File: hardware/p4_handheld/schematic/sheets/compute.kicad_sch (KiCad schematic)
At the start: 0 parts

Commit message: hw(p4_handheld): compute cluster ported, diffs clean vs card
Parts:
- added L1: 2.2uH, IND-SMD_L4.0-W4.0_HPC4018BM, symbol PSP4H:Block2
- added R3, R4: 4.7k, R0402, symbol Device:R
- added R5, R6: 10k, R0402, symbol Device:R
- added U1: ESP32-P4NRW32X, QFN-104_L10.0-W10.0-P0.35-TL-EP7.5, symbol PSP4H:Block2
- added U9: QSPI-NOR-32MB, WSON-8_L8.0-W6.10-P1.27-BL-EP, symbol PSP4H:Block2
- added X1: 40MHz-crystal, SMD3225-4P, symbol PSP4H:Block2

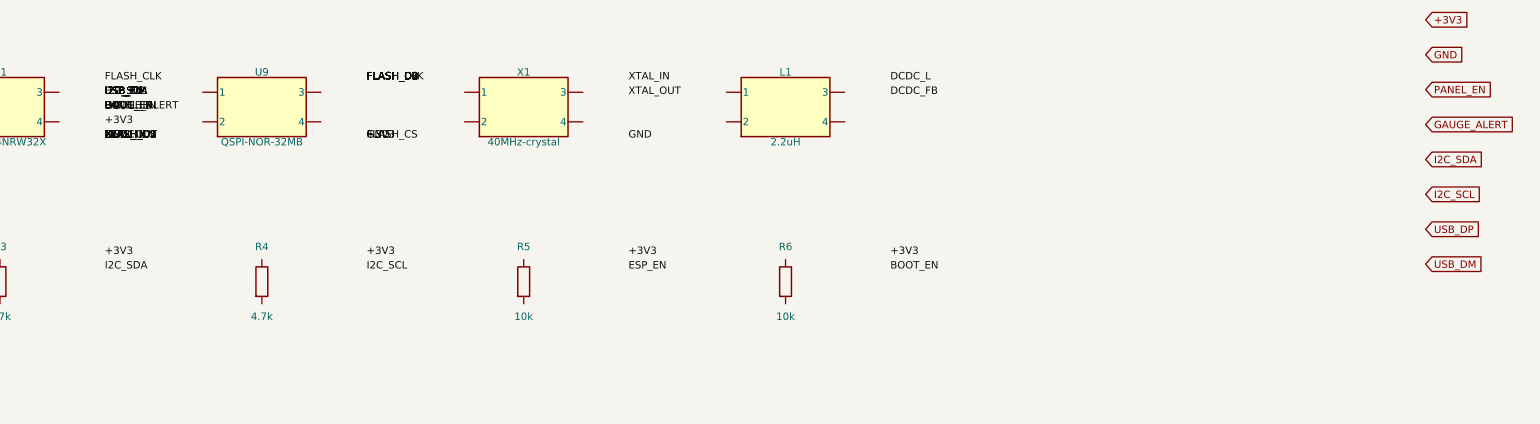
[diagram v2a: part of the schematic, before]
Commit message: hw(p4_handheld): display sheet wired to Waveshare 2.8in DSI panel
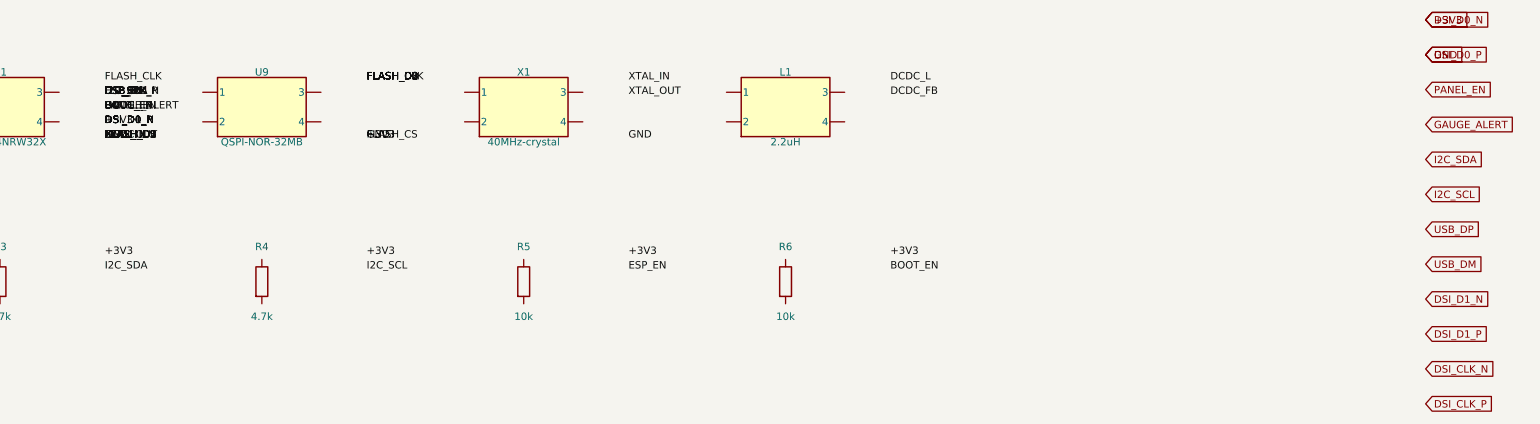
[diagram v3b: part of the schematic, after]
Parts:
- removed X1: 40MHz-crystal, SMD3225-4P, symbol PSP4H:Block2
- added R3: 4.7k, R0402, symbol Device:R
- X1: renamed from R3; value 4.7k -> 40MHz-crystal; footprint R0402 -> SMD3225-4P; symbol Device:R -> PSP4H:Block2; Gate (none) -> GATE-ESP32-P4-REF-CAPTURE; LCSC C25900 -> C9010; MPN 0402WGF4701TCE -> X322540MPB4SI
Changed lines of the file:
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@@
   (label "BOOT_EN" (at 53 35 0) (fields_autoplaced)
     (effects (font (size 1.27 1.27)) (justify left)))
+  (label "DSI_D1_N" (at 53 37.5 0) (fields_autoplaced)
+    (effects (font (size 1.27 1.27)) (justify left)))
+  (label "DSI_D1_P" (at 53 37.5 0) (fields_autoplaced)
+    (effects (font (size 1.27 1.27)) (justify left)))
+  (label "DSI_CLK_N" (at 53 32.5 0) (fields_autoplaced)
+    (effects (font (size 1.27 1.27)) (justify left)))
+  (label "DSI_CLK_P" (at 53 32.5 0) (fields_autoplaced)
+    (effects (font (size 1.27 1.27)) (justify left)))
+  (label "DSI_D0_N" (at 53 37.5 0) (fields_autoplaced)
+    (effects (font (size 1.27 1.27)) (justify left)))
+  (label "DSI_D0_P" (at 53 37.5 0) (fields_autoplaced)
+    (effects (font (size 1.27 1.27)) (justify left)))
   (symbol (lib_id "PSP4H:Block2") (at 80 35 0) (unit 1)
     (exclude_from_sim no) (in_bom yes) (on_board yes) (dnp no) (fields_autoplaced)
@@
       (effects (font (size 1.27 1.27)) hide))
   )
+  (global_label "DSI_D1_N" (shape input) (at 280 68 0) (fields_autoplaced)
+    (effects (font (size 1.27 1.27)) (justify left))
+    (property "Intersheetrefs" "${INTERSHEET_REFS}" (at 280 68 0)
+      (effects (font (size 1.27 1.27)) hide))
+  )
+  (global_label "DSI_D1_P" (shape input) (at 280 74 0) (fields_autoplaced)
+    (effects (font (size 1.27 1.27)) (justify left))
+    (property "Intersheetrefs" "${INTERSHEET_REFS}" (at 280 74 0)
+      (effects (font (size 1.27 1.27)) hide))
+  )
+  (global_label "DSI_CLK_N" (shape input) (at 280 80 0) (fields_autoplaced)
+    (effects (font (size 1.27 1.27)) (justify left))
+    (property "Intersheetrefs" "${INTERSHEET_REFS}" (at 280 80 0)
+      (effects (font (size 1.27 1.27)) hide))
+  )
+  (global_label "DSI_CLK_P" (shape input) (at 280 86 0) (fields_autoplaced)
+    (effects (font (size 1.27 1.27)) (justify left))
+    (property "Intersheetrefs" "${INTERSHEET_REFS}" (at 280 86 0)
+      (effects (font (size 1.27 1.27)) hide))
+  )
+  (global_label "DSI_D0_N" (shape input) (at 280 20 0) (fields_autoplaced)
+    (effects (font (size 1.27 1.27)) (justify left))
+    (property "Intersheetrefs" "${INTERSHEET_REFS}" (at 280 20 0)
+      (effects (font (size 1.27 1.27)) hide))
+  )
+  (global_label "DSI_D0_P" (shape input) (at 280 26 0) (fields_autoplaced)
+    (effects (font (size 1.27 1.27)) (justify left))
+    (property "Intersheetrefs" "${INTERSHEET_REFS}" (at 280 26 0)
+      (effects (font (size 1.27 1.27)) hide))
+  )

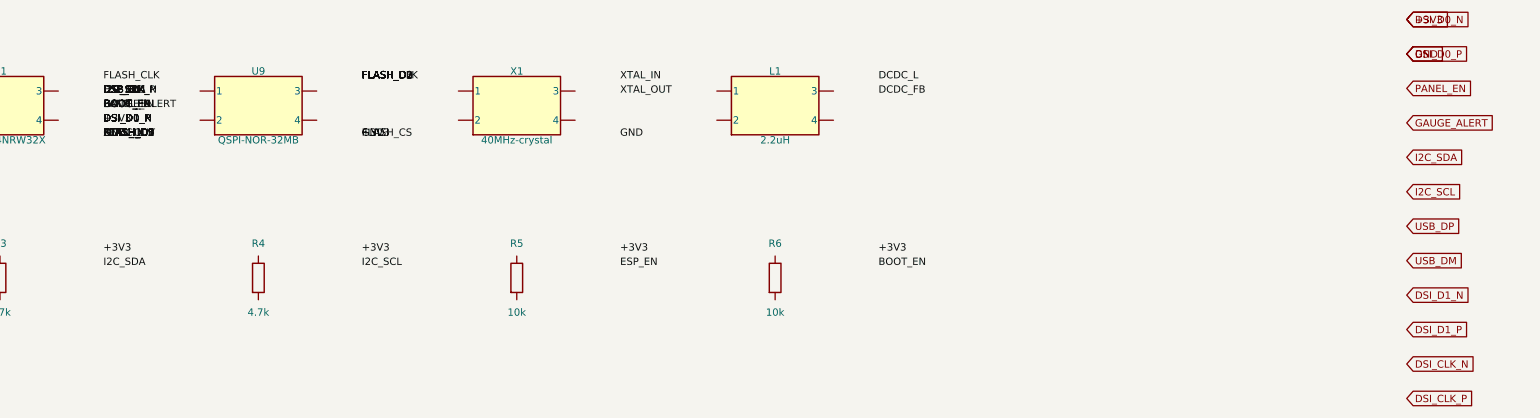
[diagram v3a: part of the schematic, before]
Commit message: hw(p4_handheld): controls sheet, 11 direct-GPIO buttons off strap pins
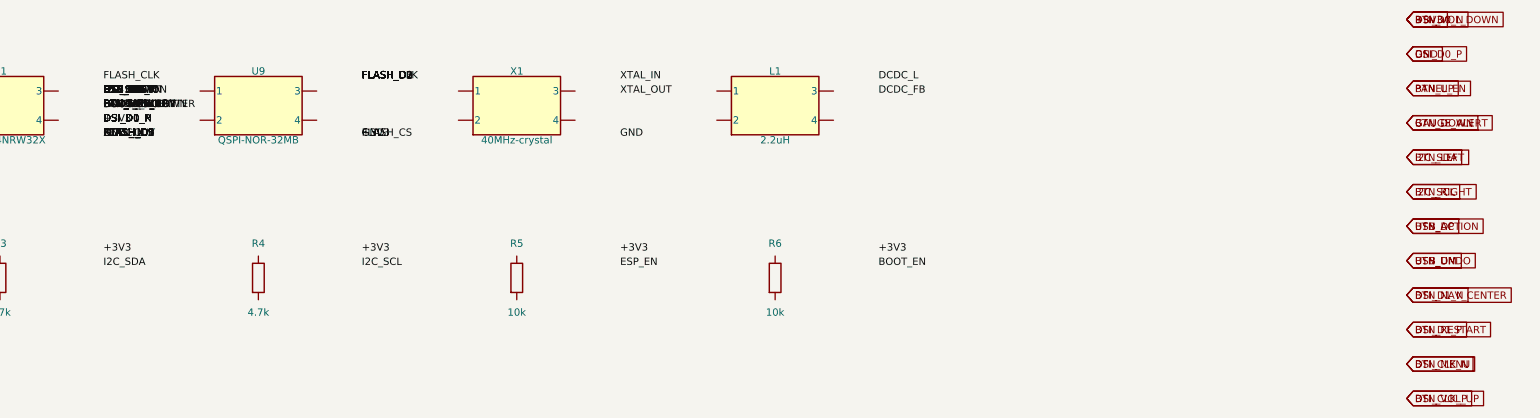
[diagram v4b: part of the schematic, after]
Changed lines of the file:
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@@
   (label "DSI_D0_P" (at 53 37.5 0) (fields_autoplaced)
     (effects (font (size 1.27 1.27)) (justify left)))
+  (label "BTN_UP" (at 53 32.5 0) (fields_autoplaced)
+    (effects (font (size 1.27 1.27)) (justify left)))
+  (label "BTN_DOWN" (at 53 32.5 0) (fields_autoplaced)
+    (effects (font (size 1.27 1.27)) (justify left)))
+  (label "BTN_LEFT" (at 53 32.5 0) (fields_autoplaced)
+    (effects (font (size 1.27 1.27)) (justify left)))
+  (label "BTN_RIGHT" (at 53 32.5 0) (fields_autoplaced)
+    (effects (font (size 1.27 1.27)) (justify left)))
+  (label "BTN_ACTION" (at 53 32.5 0) (fields_autoplaced)
+    (effects (font (size 1.27 1.27)) (justify left)))
+  (label "BTN_UNDO" (at 53 35 0) (fields_autoplaced)
+    (effects (font (size 1.27 1.27)) (justify left)))
+  (label "BTN_NAV_CENTER" (at 53 35 0) (fields_autoplaced)
+    (effects (font (size 1.27 1.27)) (justify left)))
+  (label "BTN_RESTART" (at 53 35 0) (fields_autoplaced)
+    (effects (font (size 1.27 1.27)) (justify left)))
+  (label "BTN_MENU" (at 53 35 0) (fields_autoplaced)
+    (effects (font (size 1.27 1.27)) (justify left)))
+  (label "BTN_VOL_UP" (at 53 35 0) (fields_autoplaced)
+    (effects (font (size 1.27 1.27)) (justify left)))
+  (label "BTN_VOL_DOWN" (at 53 35 0) (fields_autoplaced)
+    (effects (font (size 1.27 1.27)) (justify left)))
   (symbol (lib_id "PSP4H:Block2") (at 80 35 0) (unit 1)
     (exclude_from_sim no) (in_bom yes) (on_board yes) (dnp no) (fields_autoplaced)
@@
       (effects (font (size 1.27 1.27)) hide))
   )
+  (global_label "BTN_UP" (shape input) (at 280 32 0) (fields_autoplaced)
+    (effects (font (size 1.27 1.27)) (justify left))
+    (property "Intersheetrefs" "${INTERSHEET_REFS}" (at 280 32 0)
+      (effects (font (size 1.27 1.27)) hide))
+  )
+  (global_label "BTN_DOWN" (shape input) (at 280 38 0) (fields_autoplaced)
+    (effects (font (size 1.27 1.27)) (justify left))
+    (property "Intersheetrefs" "${INTERSHEET_REFS}" (at 280 38 0)
+      (effects (font (size 1.27 1.27)) hide))
+  )
+  (global_label "BTN_LEFT" (shape input) (at 280 44 0) (fields_autoplaced)
+    (effects (font (size 1.27 1.27)) (justify left))
+    (property "Intersheetrefs" "${INTERSHEET_REFS}" (at 280 44 0)
+      (effects (font (size 1.27 1.27)) hide))
+  )
+  (global_label "BTN_RIGHT" (shape input) (at 280 50 0) (fields_autoplaced)
+    (effects (font (size 1.27 1.27)) (justify left))
+    (property "Intersheetrefs" "${INTERSHEET_REFS}" (at 280 50 0)
+      (effects (font (size 1.27 1.27)) hide))
+  )
+  (global_label "BTN_ACTION" (shape input) (at 280 56 0) (fields_autoplaced)
+    (effects (font (size 1.27 1.27)) (justify left))
+    (property "Intersheetrefs" "${INTERSHEET_REFS}" (at 280 56 0)
+      (effects (font (size 1.27 1.27)) hide))
+  )
+  (global_label "BTN_UNDO" (shape input) (at 280 62 0) (fields_autoplaced)
+    (effects (font (size 1.27 1.27)) (justify left))
+    (property "Intersheetrefs" "${INTERSHEET_REFS}" (at 280 62 0)
+      (effects (font (size 1.27 1.27)) hide))
+  )
+  (global_label "BTN_NAV_CENTER" (shape input) (at 280 68 0) (fields_autoplaced)
+    (effects (font (size 1.27 1.27)) (justify left))
+    (property "Intersheetrefs" "${INTERSHEET_REFS}" (at 280 68 0)
+      (effects (font (size 1.27 1.27)) hide))
+  )
+  (global_label "BTN_RESTART" (shape input) (at 280 74 0) (fields_autoplaced)
+    (effects (font (size 1.27 1.27)) (justify left))
+    (property "Intersheetrefs" "${INTERSHEET_REFS}" (at 280 74 0)
+      (effects (font (size 1.27 1.27)) hide))
+  )
+  (global_label "BTN_MENU" (shape input) (at 280 80 0) (fields_autoplaced)
+    (effects (font (size 1.27 1.27)) (justify left))
+    (property "Intersheetrefs" "${INTERSHEET_REFS}" (at 280 80 0)
+      (effects (font (size 1.27 1.27)) hide))
+  )
+  (global_label "BTN_VOL_UP" (shape input) (at 280 86 0) (fields_autoplaced)
+    (effects (font (size 1.27 1.27)) (justify left))
+    (property "Intersheetrefs" "${INTERSHEET_REFS}" (at 280 86 0)
+      (effects (font (size 1.27 1.27)) hide))
+  )
+  (global_label "BTN_VOL_DOWN" (shape input) (at 280 20 0) (fields_autoplaced)
+    (effects (font (size 1.27 1.27)) (justify left))
+    (property "Intersheetrefs" "${INTERSHEET_REFS}" (at 280 20 0)
+      (effects (font (size 1.27 1.27)) hide))
+  )

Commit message: hw(p4_handheld): audio, storage, debug sheets
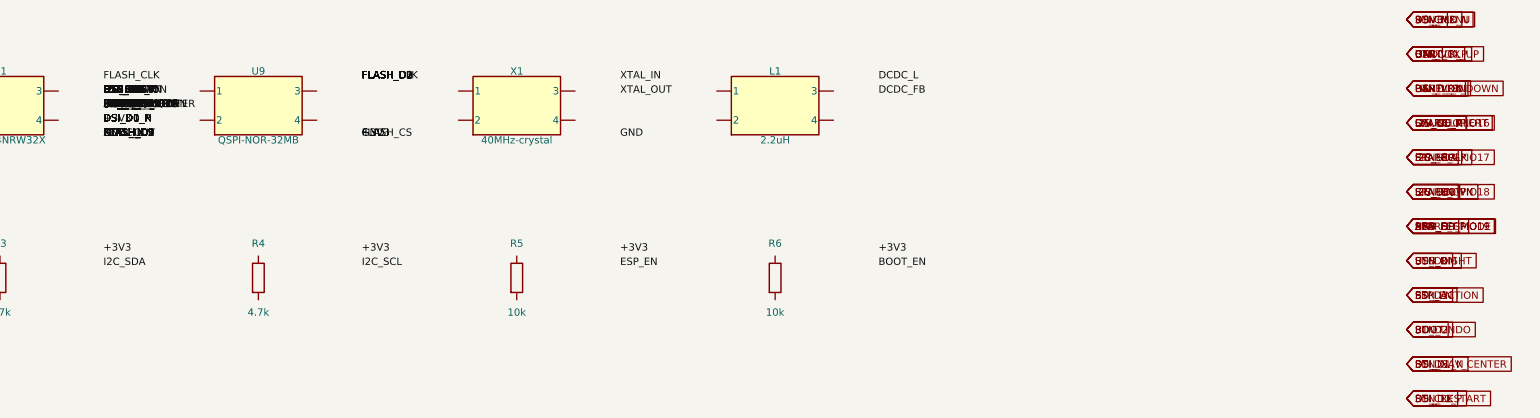
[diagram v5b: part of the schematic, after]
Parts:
- removed U9: QSPI-NOR-32MB, WSON-8_L8.0-W6.10-P1.27-BL-EP, symbol PSP4H:Block2
- removed X1: 40MHz-crystal, SMD3225-4P, symbol PSP4H:Block2
- added R3: 4.7k, R0402, symbol Device:R
- added R6: 10k, R0402, symbol Device:R
- U9: renamed from R3; value 4.7k -> QSPI-NOR-32MB; footprint R0402 -> WSON-8_L8.0-W6.10-P1.27-BL-EP; symbol Device:R -> PSP4H:Block2; Gate (none) -> GATE-ESP32-P4-REF-CAPTURE; LCSC C25900 -> C97522; MPN 0402WGF4701TCE -> W25Q256JVEIQ
- X1: renamed from R6; value 10k -> 40MHz-crystal; footprint R0402 -> SMD3225-4P; symbol Device:R -> PSP4H:Block2; Gate (none) -> GATE-ESP32-P4-REF-CAPTURE; LCSC C25744 -> C9010; MPN 0402WGF1002TCE -> X322540MPB4SI
